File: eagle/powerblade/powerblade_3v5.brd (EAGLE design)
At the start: 25.4 x 25.4 mm, 78 parts, among them J1 JTAG_14PIN_IDC-ND, J2 AC_INFINAL, J4 TC2030-JLINK-NL, Q1 NTS4173, Q4 2SK1829, U1 TPS62122, U2 MCP6V3, U3 MSP430FR5738, U4 NRF51822QF, U6 MAX9910, U7 OPA2369, X1 16MHz, X3 32.768kHz, Y1 UREACH_XTEND

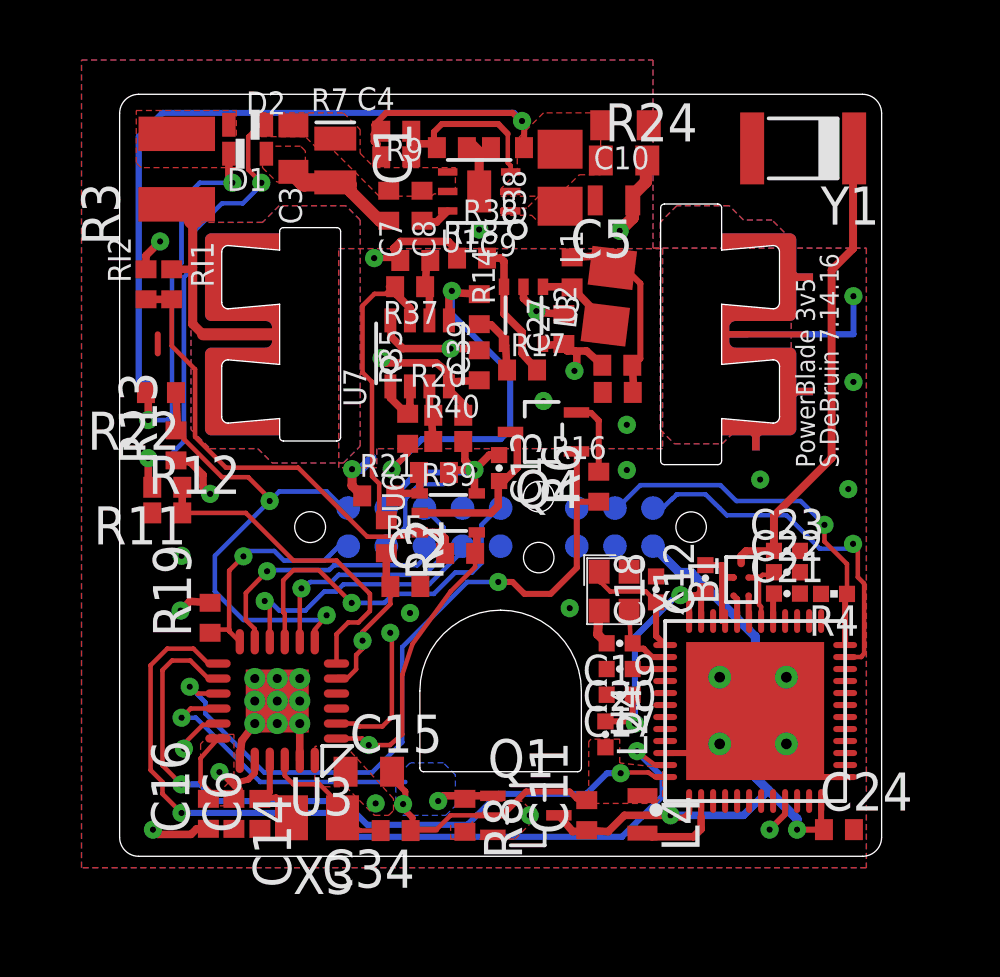
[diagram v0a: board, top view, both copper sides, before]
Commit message: updated powerblade to use new cutouts
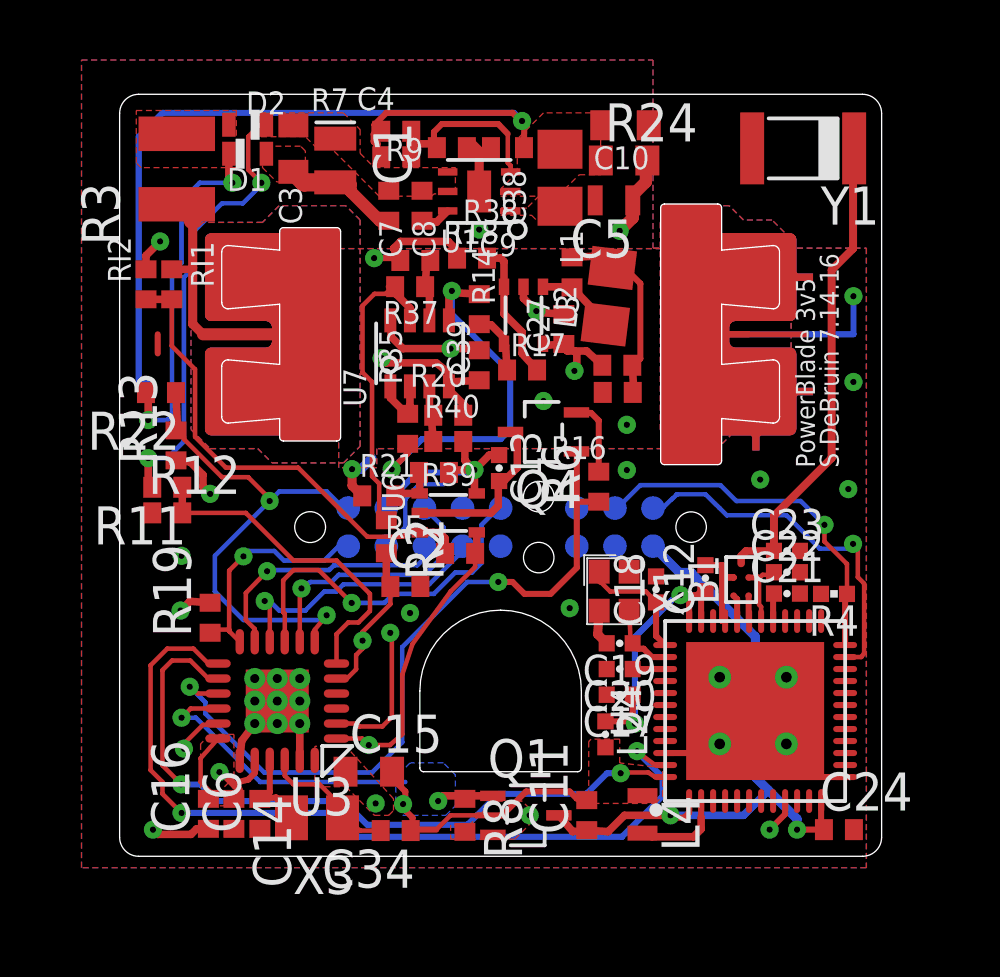
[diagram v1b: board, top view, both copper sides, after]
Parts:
- J2: value AC_INFINAL -> AC_IN51; device powerfilm:AC3_FINAL -> powerfilm:AC3_51
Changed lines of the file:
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@@
 <attribute name="DIGIKEY" value="490-4025-1-ND" x="4.727575" y="-16.002" size="1.778" layer="27" rot="R270" display="off"/>
 </element>
-<element name="J2" library="powerfilm" package="AC3_FINAL" value="AC_INFINAL" x="0" y="0">
+<element name="J2" library="powerfilm" package="AC3_51" value="AC_IN51" x="0" y="0">
 <attribute name="DIGIKEY" value="ED1649-ND" x="0" y="0" size="1.778" layer="27" display="off"/>
 <attribute name="DIGIKEY_2" value="ED1649-ND" x="0" y="0" size="1.778" layer="27" display="off"/>
